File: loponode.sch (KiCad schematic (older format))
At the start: 20 parts

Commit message: some fixes, annotations, associations
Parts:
- removed J?: Conn_01x08_Female, symbol Connector:Conn_01x08_Female
- removed J?: Conn_01x02, symbol Connector_Generic:Conn_01x02
- C1, C2, C8, C9: renamed from C?; footprint (none) -> Capacitor_SMD:C_0805_2012Metric_Pad1.15x1.40mm_HandSolder
- C3, C4, C5, C6, C7: renamed from C?; value 22u -> 100n; footprint (none) -> Capacitor_SMD:C_0805_2012Metric_Pad1.15x1.40mm_HandSolder
- J1: renamed from J?; value Conn_02x05_Odd_Even -> DEBUG; footprint (none) -> Connector_PinHeader_2.54mm:PinHeader_2x05_P2.54mm_Vertical
- JP1, JP2: renamed from JP?; footprint (none) -> Jumper:SolderJumper-2_P1.3mm_Open_TrianglePad1.0x1.5mm
- L1: renamed from L?; value L -> 4,7uH
- R1: renamed from R?; footprint (none) -> Resistor_SMD:R_0805_2012Metric_Pad1.15x1.40mm_HandSolder
- gave numbers to parts that had none: 4
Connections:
- net SCL: now also U2.45 (PB8)
- net SDA: now also U2.46 (PB9)
- net GPIO_PA15: now reaches U2.38 (PA15)
- net GPIO_PB3: now reaches U2.39 (PB3)
- net GPIO_PB4: now reaches U2.40 (PB4)
- net GPIO_PB5: now reaches U2.41 (PB5)
- net SWIM: no longer names the net of J1.5 (Pin_5)
- no-connect marks 2 -> 18

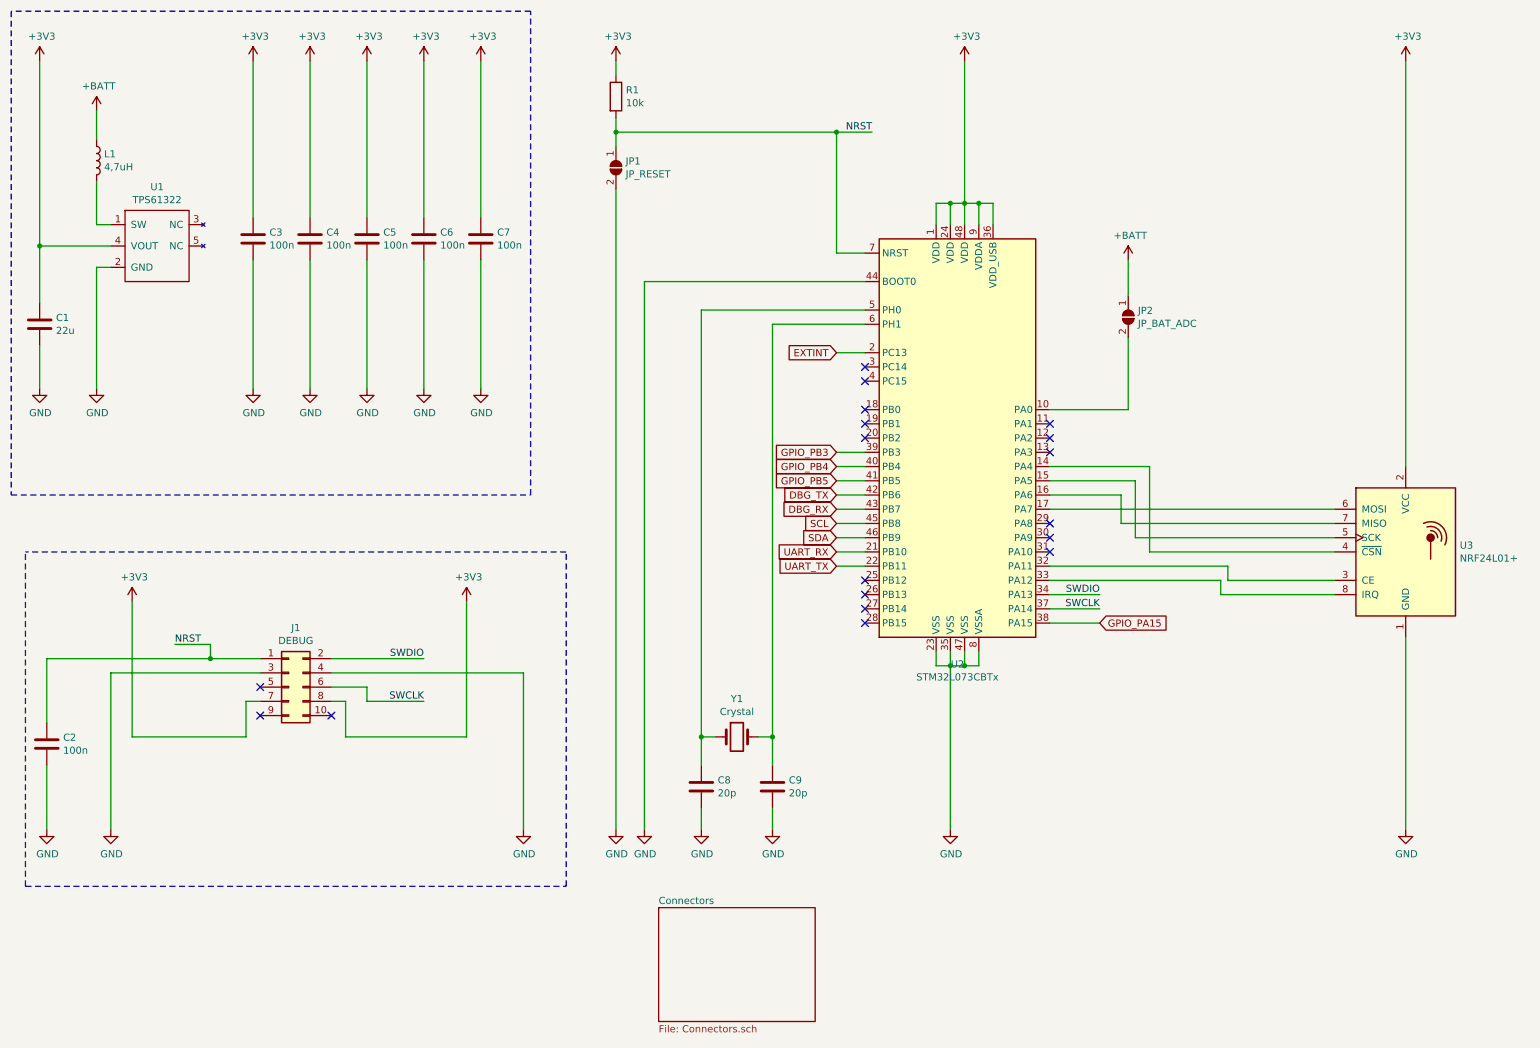
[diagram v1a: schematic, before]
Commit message: add jumper for power measurement; format GND a bit better
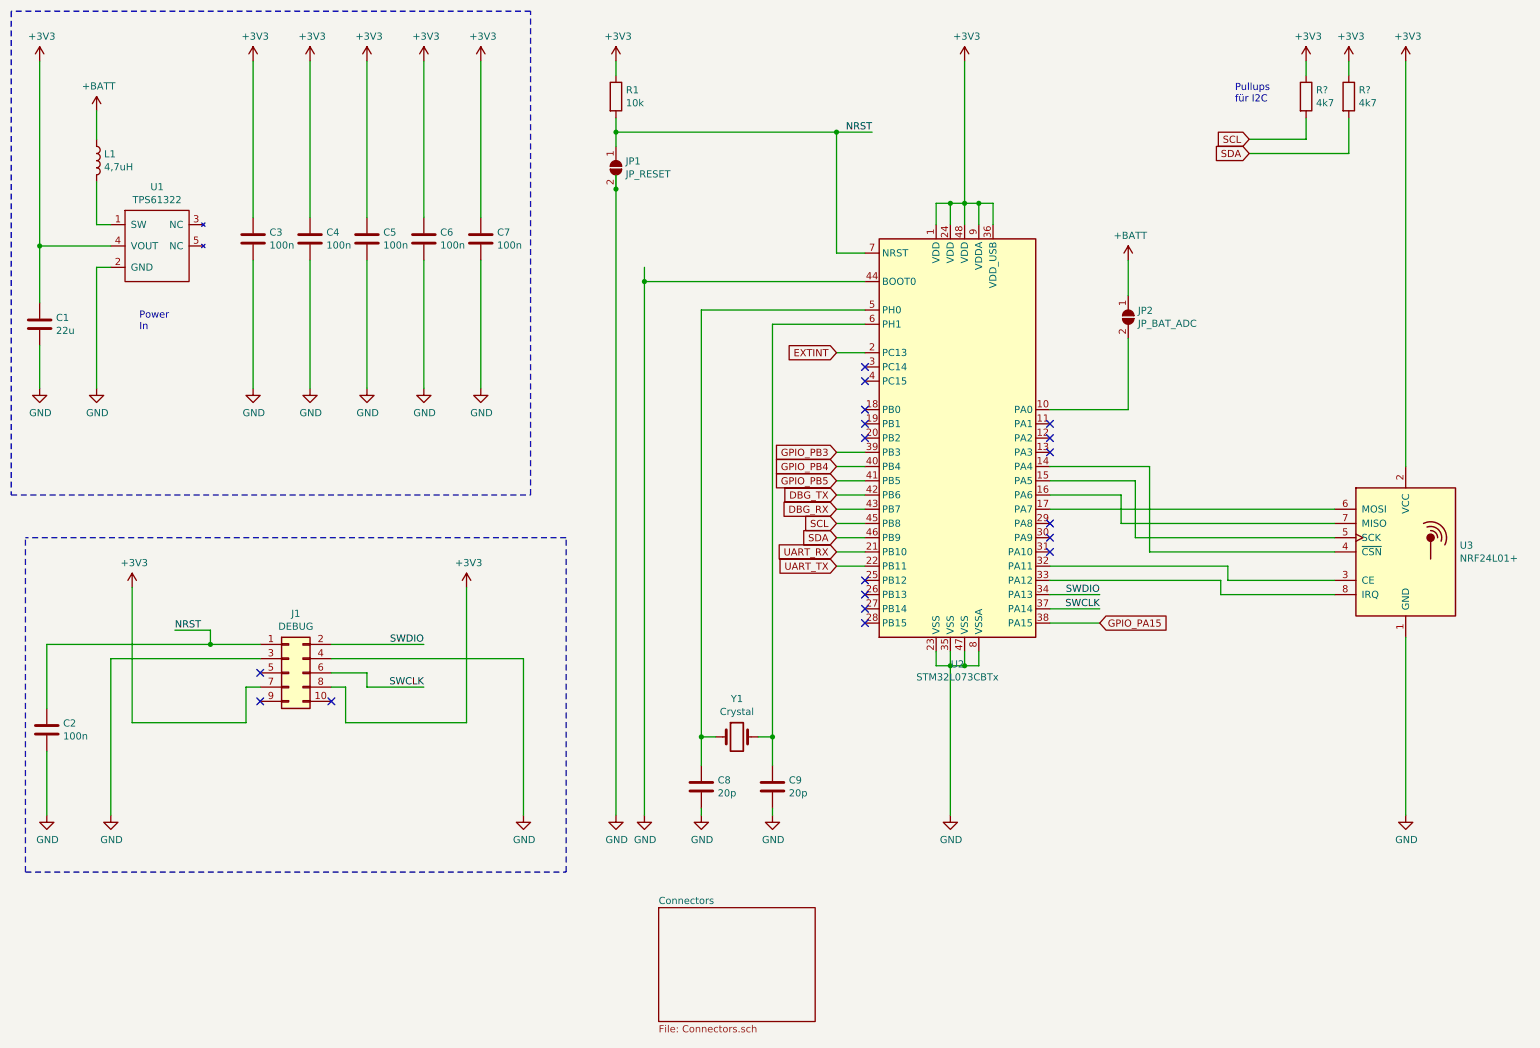
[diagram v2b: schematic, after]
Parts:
- added R? (x2): 4k7, symbol Device:R
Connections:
- net +3V3: now also R?.1, R?.1
- net SCL: now also R?.2
- net SDA: now also R?.2
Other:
- note added: "Power\nIn"
- note added: "Pullups\nfür I2C"
- moved on the sheet: C2, J1

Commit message: some more annotations
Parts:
- L1: footprint (none) -> Inductor_SMD:L_1210_3225Metric_Pad1.42x2.65mm_HandSolder
- R2, R3: renamed from R?; footprint (none) -> Resistor_SMD:R_0805_2012Metric_Pad1.15x1.40mm_HandSolder
- U1: footprint (none) -> SOT95P280X145-5N:SOT95P280X145-5N
- Y1: footprint (none) -> Crystal:Crystal_SMD_HC49-SD_HandSoldering
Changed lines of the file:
@@
 F 0 "U1" H 1625 2665 50  0000 C CNN
 F 1 "TPS61322" H 1625 2574 50  0000 C CNN
-F 2 "" H 1100 2950 50  0001 C CNN
+F 2 "SOT95P280X145-5N:SOT95P280X145-5N" H 1100 2950 50  0001 C CNN
 F 3 "" H 1100 2950 50  0001 C CNN
 	1    1600 2250
@@
 F 0 "L1" H 1253 1696 50  0000 L CNN
 F 1 "4,7uH" H 1253 1605 50  0000 L CNN
-F 2 "" H 1200 1650 50  0001 C CNN
+F 2 "Inductor_SMD:L_1210_3225Metric_Pad1.42x2.65mm_HandSolder" H 1200 1650 50  0001 C CNN
 F 3 "~" H 1200 1650 50  0001 C CNN
 	1    1200 1650
@@
 	4850 1450 4850 1350
 Wire Wire Line
-	4850 1750 4850 1850
-Wire Wire Line
 	7900 4700 8250 4700
 Wire Wire Line
@@
 F 0 "Y1" H 5700 5968 50  0000 C CNN
 F 1 "Crystal" H 5700 5877 50  0000 C CNN
-F 2 "" H 5700 5700 50  0001 C CNN
+F 2 "Crystal:Crystal_SMD_HC49-SD_HandSoldering" H 5700 5700 50  0001 C CNN
 F 3 "~" H 5700 5700 50  0001 C CNN
 	1    5700 5700
@@
 NoConn ~ 2350 5250
 $Comp
-L power:+3V3 #PWR?
+L power:+3V3 #PWR0130
 U 1 1 5D17FC61
 P 10000 950
-F 0 "#PWR?" H 10000 800 50  0001 C CNN
+F 0 "#PWR0130" H 10000 800 50  0001 C CNN
 F 1 "+3V3" H 10015 1123 50  0000 C CNN
 F 2 "" H 10000 950 50  0001 C CNN
@@
 $EndComp
 $Comp
-L power:+3V3 #PWR?
+L power:+3V3 #PWR0138
 U 1 1 5D180087
 P 9700 950
-F 0 "#PWR?" H 9700 800 50  0001 C CNN
+F 0 "#PWR0138" H 9700 800 50  0001 C CNN
 F 1 "+3V3" H 9715 1123 50  0000 C CNN
 F 2 "" H 9700 950 50  0001 C CNN
@@
 SDA
 $Comp
-L Device:R R?
+L Device:R R2
 U 1 1 5D192CDF
 P 9700 1200
-F 0 "R?" H 9770 1246 50  0000 L CNN
+F 0 "R2" H 9770 1246 50  0000 L CNN
 F 1 "4k7" H 9770 1155 50  0000 L CNN
-F 2 "" V 9630 1200 50  0001 C CNN
+F 2 "Resistor_SMD:R_0805_2012Metric_Pad1.15x1.40mm_HandSolder" V 9630 1200 50  0001 C CNN
 F 3 "~" H 9700 1200 50  0001 C CNN
 	1    9700 1200
@@
 $EndComp
 $Comp
-L Device:R R?
+L Device:R R3
 U 1 1 5D1932F5
 P 10000 1200
-F 0 "R?" H 10070 1246 50  0000 L CNN
+F 0 "R3" H 10070 1246 50  0000 L CNN
 F 1 "4k7" H 10070 1155 50  0000 L CNN
-F 2 "" V 9930 1200 50  0001 C CNN
+F 2 "Resistor_SMD:R_0805_2012Metric_Pad1.15x1.40mm_HandSolder" V 9930 1200 50  0001 C CNN
 F 3 "~" H 10000 1200 50  0001 C CNN
 	1    10000 1200
@@
 Text Notes 1500 2850 0    50   ~ 0
 Power\nIn
-Connection ~ 4850 1850
 Wire Wire Line
 	4850 1850 4850 6250
-Connection ~ 5050 2500
-Wire Wire Line
-	5050 2500 5050 2400
 Wire Wire Line
 	5450 6200 5450 6250

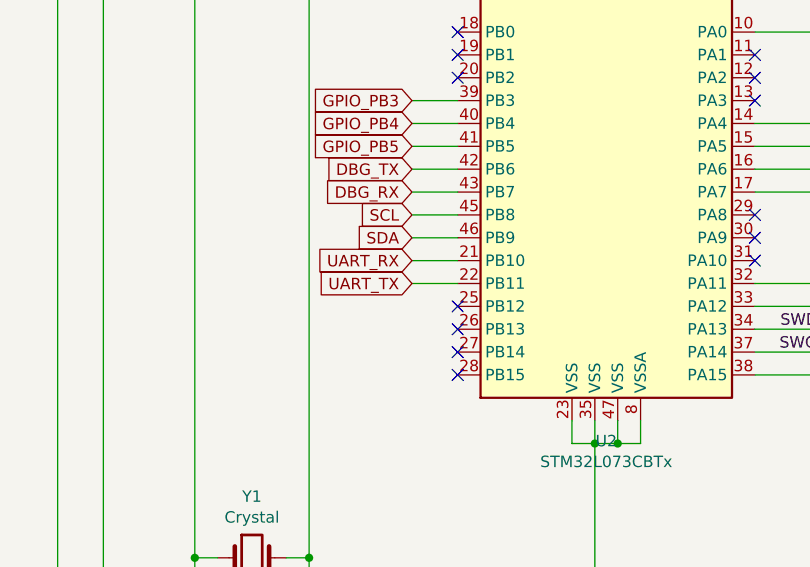
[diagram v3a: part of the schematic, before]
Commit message: add some wires
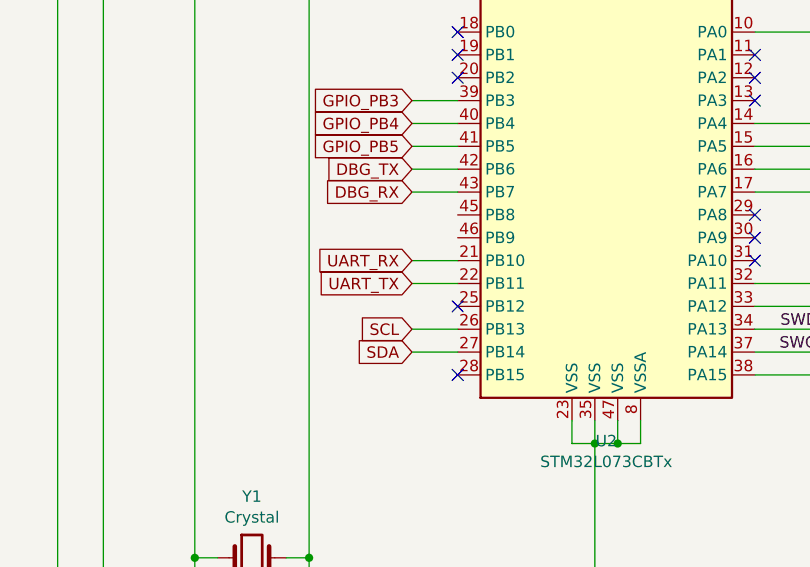
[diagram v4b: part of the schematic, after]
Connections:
- net SCL: now also U2.26 (PB13); no longer U2.45 (PB8)
- net SDA: now also U2.27 (PB14); no longer U2.46 (PB9)
- no-connect marks 18 -> 16
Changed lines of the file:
@@
 $EndDescr
-$Comp
-L MCU_ST_STM32L0:STM32L073CBTx U2
-U 1 1 5CFFD9E1
-P 7300 3600
-F 0 "U2" H 7250 2011 50  0000 C CNN
-F 1 "STM32L073CBTx" H 7250 1920 50  0000 C CNN
-F 2 "Package_QFP:LQFP-48_7x7mm_P0.5mm" H 6700 2200 50  0001 R CNN
-F 3 "http://www.st.com/st-web-ui/static/active/en/resource/technical/document/datasheet/DM00141036.pdf" H 7300 3600 50  0001 C CNN
-	1    7300 3600
-	1    0    0    -1
-$EndComp
 $Comp
 L RF:NRF24L01_Breakout U3
@@
 Wire Wire Line
 	6400 3000 6600 3000
-Text GLabel 6400 4200 0    50   Input ~ 0
+Text GLabel 6400 4700 0    50   Input ~ 0
 SCL
-Text GLabel 6400 4300 0    50   Input ~ 0
+Text GLabel 6400 4800 0    50   Input ~ 0
 SDA
-Wire Wire Line
-	6400 4300 6600 4300
-Wire Wire Line
-	6600 4200 6400 4200
 Text GLabel 6400 3700 0    50   Input ~ 0
 GPIO_PB3
@@
 NoConn ~ 6600 3600
 NoConn ~ 6600 4600
-NoConn ~ 6600 4700
-NoConn ~ 6600 4800
 NoConn ~ 6600 4900
 NoConn ~ 7900 4400
@@
 Wire Wire Line
 	10400 5000 10400 6250
+$Comp
+L MCU_ST_STM32L0:STM32L073CBTx U2
+U 1 1 5CFFD9E1
+P 7300 3600
+F 0 "U2" H 7250 2011 50  0000 C CNN
+F 1 "STM32L073CBTx" H 7250 1920 50  0000 C CNN
+F 2 "Package_QFP:LQFP-48_7x7mm_P0.5mm" H 6700 2200 50  0001 R CNN
+F 3 "http://www.st.com/st-web-ui/static/active/en/resource/technical/document/datasheet/DM00141036.pdf" H 7300 3600 50  0001 C CNN
+	1    7300 3600
+	1    0    0    -1
+$EndComp
+Wire Wire Line
+	6400 4700 6600 4700
+Wire Wire Line
+	6600 4800 6400 4800
 $EndSCHEMATC

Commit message: many optimizations; LAYOUT!
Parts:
- removed Y1: Crystal, Crystal:Crystal_SMD_HC49-SD_HandSoldering, symbol Device:Crystal
- added Y1: 8MHz, Crystal:Crystal_SMD_EuroQuartz_MQ-4Pin_7.0x5.0mm_HandSoldering, symbol Device:Crystal_GND24_Small
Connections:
- net GND: now also Y1.2, Y1.4
- net at U2.10 (PA0): now also U3.8 (IRQ); no longer JP2.2 (B)
- net at U2.11 (PA1): now also JP2.2 (B)
- net RF_CE: now reaches U2.20 (PB2)
- net RF_CE: now also U3.3 (CE)
- net at U2.32 (PA11): no longer U3.3 (CE)
- net at U2.33 (PA12): no longer U3.8 (IRQ)
- net at C8.1, U2.5 (PH0): now also Y1.1
- net at C9.1, U2.6 (PH1): now also Y1.3
- no-connect marks 16 -> 18
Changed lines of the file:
@@
 	5050 2500 6600 2500
-$Comp
-L Device:Crystal Y1
-U 1 1 5D2205E1
-P 5700 5700
-F 0 "Y1" H 5700 5968 50  0000 C CNN
-F 1 "Crystal" H 5700 5877 50  0000 C CNN
-F 2 "Crystal:Crystal_SMD_HC49-SD_HandSoldering" H 5700 5700 50  0001 C CNN
-F 3 "~" H 5700 5700 50  0001 C CNN
-	1    5700 5700
-	1    0    0    -1
-$EndComp
 $Comp
 L power:GND #PWR0127
@@
 $EndComp
 Wire Wire Line
-	5950 5900 5950 5700
-Wire Wire Line
-	5950 5700 5850 5700
-Wire Wire Line
-	5550 5700 5450 5700
-Wire Wire Line
-	5450 5700 5450 5900
-Wire Wire Line
-	5450 5700 5450 2700
-Wire Wire Line
 	5450 2700 6600 2700
-Connection ~ 5450 5700
 Wire Wire Line
 	6600 2800 5950 2800
 Wire Wire Line
-	5950 2800 5950 5700
-Connection ~ 5950 5700
-Wire Wire Line
-	7900 4500 9150 4500
-Wire Wire Line
-	9150 4500 9150 4600
-Wire Wire Line
-	9100 4700 9100 4600
-Wire Wire Line
-	9100 4600 7900 4600
-Wire Wire Line
 	7900 4100 9900 4100
 Wire Wire Line
@@
 Wire Wire Line
 	8600 4400 9900 4400
-Wire Wire Line
-	9150 4600 9900 4600
-Wire Wire Line
-	9100 4700 9900 4700
 $Comp
 L power:+BATT #PWR0129
@@
 	1    0    0    -1
 $EndComp
-Wire Wire Line
-	7900 3400 8450 3400
 $Comp
 L Jumper:SolderJumper_2_Open JP2
@@
 Wire Wire Line
 	8450 2350 8450 2600
-Wire Wire Line
-	8450 2900 8450 3400
 $Sheet
 S 5150 6900 1100 800
@@
 NoConn ~ 6600 3400
 NoConn ~ 6600 3500
-NoConn ~ 6600 3600
 NoConn ~ 6600 4600
 NoConn ~ 6600 4900
@@
 NoConn ~ 7900 3700
 NoConn ~ 7900 3600
-NoConn ~ 7900 3500
 Text Label 8250 4700 2    50   ~ 0
 SWDIO
@@
 Wire Wire Line
 	6600 4800 6400 4800
+Text Label 6250 3600 0    50   ~ 0
+RF_CE
+Wire Wire Line
+	6250 3600 6600 3600
+Text Label 9500 4600 0    50   ~ 0
+RF_CE
+Wire Wire Line
+	9500 4600 9900 4600
+Wire Wire Line
+	7900 3400 8700 3400
+Wire Wire Line
+	8700 3400 8700 4700
+Wire Wire Line
+	8700 4700 9900 4700
+Wire Wire Line
+	7900 3500 8450 3500
+Wire Wire Line
+	8450 3500 8450 2900
+NoConn ~ 7900 4500
+NoConn ~ 7900 4600
+NoConn ~ 6600 4300
+NoConn ~ 6600 4200
+$Comp
+L Device:Crystal_GND24_Small Y1
+U 1 1 5D1CF045
+P 5700 5700
+F 0 "Y1" H 5844 5746 50  0000 L CNN
+F 1 "8MHz" H 5844 5655 50  0000 L CNN
+F 2 "Crystal:Crystal_SMD_EuroQuartz_MQ-4Pin_7.0x5.0mm_HandSoldering" H 5700 5700 50  0001 C CNN
+F 3 "~" H 5700 5700 50  0001 C CNN
+	1    5700 5700
+	1    0    0    -1
+$EndComp
+Wire Wire Line
+	5950 2800 5950 5700
+Wire Wire Line
+	5450 2700 5450 5700
+Wire Wire Line
+	5600 5700 5450 5700
+Connection ~ 5450 5700
+Wire Wire Line
+	5450 5700 5450 5900
+Wire Wire Line
+	5800 5700 5950 5700
+Connection ~ 5950 5700
+Wire Wire Line
+	5950 5700 5950 5900
+$Comp
+L power:GND #PWR0140
+U 1 1 5D1F5009
+P 5750 6250
+F 0 "#PWR0140" H 5750 6000 50  0001 C CNN
+F 1 "GND" H 5755 6077 50  0000 C CNN
+F 2 "" H 5750 6250 50  0001 C CNN
+F 3 "" H 5750 6250 50  0001 C CNN
+	1    5750 6250
+	1    0    0    -1
+$EndComp
+$Comp
+L power:GND #PWR0141
+U 1 1 5D1F521F
+P 6300 6250
+F 0 "#PWR0141" H 6300 6000 50  0001 C CNN
+F 1 "GND" H 6305 6077 50  0000 C CNN
+F 2 "" H 6300 6250 50  0001 C CNN
+F 3 "" H 6300 6250 50  0001 C CNN
+	1    6300 6250
+	1    0    0    -1
+$EndComp
+Wire Wire Line
+	5750 6250 5750 5900
+Wire Wire Line
+	5750 5900 5700 5900
+Wire Wire Line
+	5700 5900 5700 5800
+Wire Wire Line
+	5700 5600 5700 5500
+Wire Wire Line
+	5700 5500 6300 5500
+Wire Wire Line
+	6300 5500 6300 6250
 $EndSCHEMATC
